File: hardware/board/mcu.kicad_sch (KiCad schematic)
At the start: 22 parts

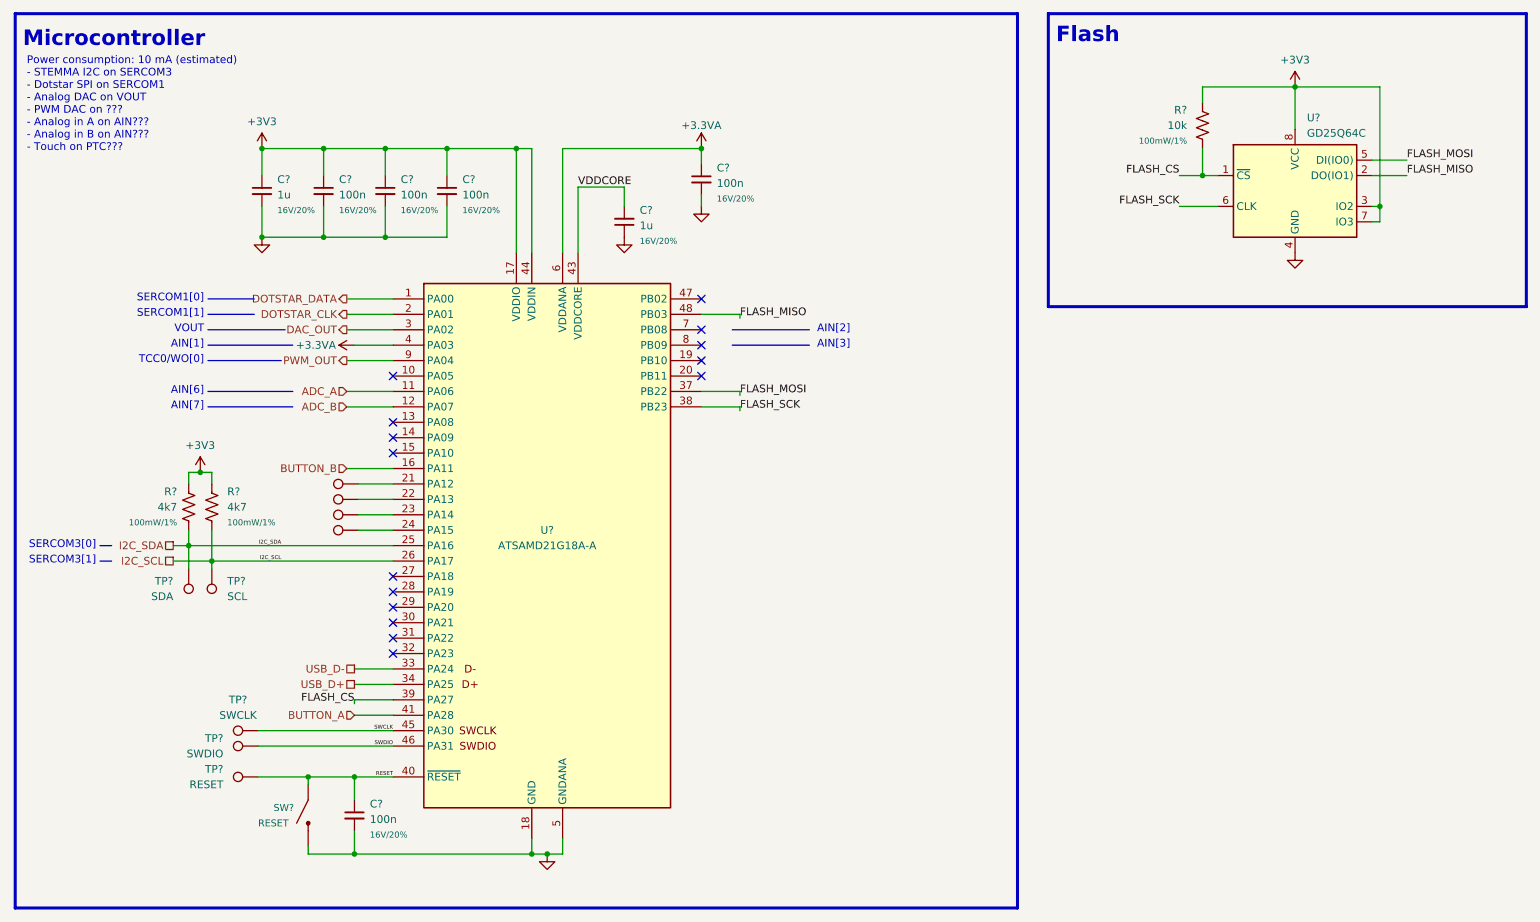
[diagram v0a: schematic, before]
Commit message: hardware: change USB connector, change flash chip, change SPI flash pin assignments, other small updates to routing
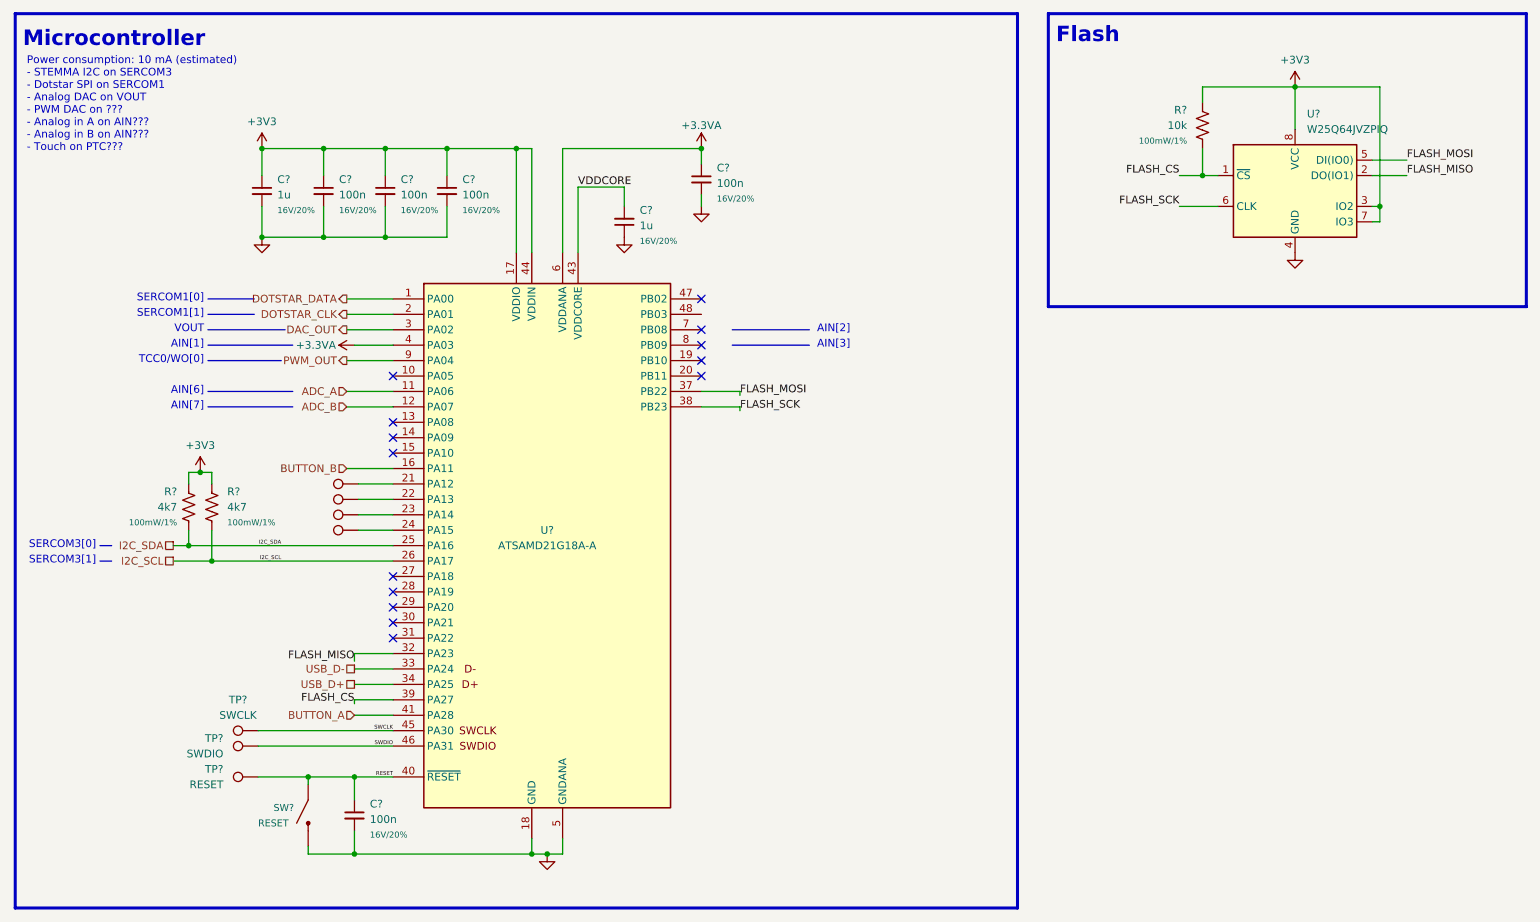
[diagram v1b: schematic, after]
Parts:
- removed TP?: SCL, TestPoint:TestPoint_Pad_D1.0mm, symbol Connector:TestPoint
- removed TP?: SDA, TestPoint:TestPoint_Pad_D1.0mm, symbol Connector:TestPoint
- U?: value GD25Q64C -> W25Q64JVZPIQ; footprint Package_SO:SOIC-8_5.23x5.23mm_P1.27mm -> Package_SON:WSON-8-1EP_6x5mm_P1.27mm_EP3.4x4mm; mfn GD25Q64CSIGR -> (none); mpn GD25Q64CSIGR -> W25Q64JVZPIQ
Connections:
- net FLASH_MISO: now also U?.32 (PA23); no longer U?.48 (PB03)
- no-connect marks 15 -> 14
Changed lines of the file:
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@@
   )
   (no_connect (at 128.27 72.39))
-  (no_connect (at 77.47 120.65))
   (no_connect (at 77.47 115.57))
-  (no_connect (at 77.47 118.11))
+  (no_connect (at 77.47 113.03))
   (no_connect (at 77.47 85.09))
   (no_connect (at 77.47 107.95))
@@
   (no_connect (at 77.47 82.55))
   (no_connect (at 77.47 87.63))
-  (no_connect (at 77.47 113.03))
+  (no_connect (at 77.47 118.11))
   (no_connect (at 128.27 67.31))
   (no_connect (at 128.27 69.85))
@@
     (stroke (width 0) (type default))
   )
-  (wire (pts (xy 47.625 106.68) (xy 47.625 105.41))
-    (stroke (width 0) (type default))
-  )
   (wire (pts (xy 128.27 45.085) (xy 128.27 46.99))
     (stroke (width 0) (type default))
@@
     (stroke (width 0) (type default))
   )
-  (wire (pts (xy 134.62 64.77) (xy 128.27 64.77))
+  (wire (pts (xy 71.12 120.65) (xy 77.47 120.65))
     (stroke (width 0) (type default))
   )
@@
     (stroke (width 0.5) (type solid))
   )
-  (wire (pts (xy 43.815 102.87) (xy 43.815 106.68))
-    (stroke (width 0) (type default))
-  )
   (polyline (pts (xy 180.34 162.56) (xy 15.24 162.56))
     (stroke (width 0.5) (type solid))
@@
     (stroke (width 0) (type default))
   )
-  (wire (pts (xy 134.62 64.77) (xy 134.62 65.405))
+  (wire (pts (xy 71.12 120.65) (xy 71.12 121.92))
     (stroke (width 0) (type default))
   )
@@
     (effects (font (size 1.27 1.27)) (justify right bottom))
   )
-  (label "FLASH_MISO" (at 134.62 65.405 0) (fields_autoplaced)
-    (effects (font (size 1.27 1.27)) (justify left bottom))
+  (label "FLASH_MISO" (at 71.12 121.92 180) (fields_autoplaced)
+    (effects (font (size 1.27 1.27)) (justify right bottom))
   )
   (label "FLASH_CS" (at 71.12 128.905 180) (fields_autoplaced)
@@
   (symbol (lib_id "board:GD25Q64C") (at 226.06 44.45 0) (unit 1)
     (in_bom yes) (on_board yes) (dnp no) (fields_autoplaced)
-    (property "Reference" "U?" (at 228.0159 32.385 0)
-      (effects (font (size 1.27 1.27)) (justify left))
-    )
-    (property "Value" "GD25Q64C" (at 228.0159 34.925 0)
-      (effects (font (size 1.27 1.27)) (justify left))
-    )
-    (property "Footprint" "Package_SO:SOIC-8_5.23x5.23mm_P1.27mm" (at 226.06 44.45 0)
-      (effects (font (size 1.27 1.27)) hide)
-    )
-    (property "Datasheet" "http://www.winbond.com/resource-files/w25q32jv%20revg%2003272018%20plus.pdf" (at 226.06 44.45 0)
-      (effects (font (size 1.27 1.27)) hide)
-    )
-    (property "mfn" "GD25Q64CSIGR" (at 226.06 44.45 0)
-      (effects (font (size 1.27 1.27)) hide)
-    )
-    (property "mpn" "GD25Q64CSIGR" (at 226.06 44.45 0)
+    (property "Reference" "U?" (at 228.0159 31.75 0)
+      (effects (font (size 1.27 1.27)) (justify left))
+    )
+    (property "Value" "W25Q64JVZPIQ" (at 228.0159 34.29 0)
+      (effects (font (size 1.27 1.27)) (justify left))
+    )
+    (property "Footprint" "Package_SON:WSON-8-1EP_6x5mm_P1.27mm_EP3.4x4mm" (at 226.06 44.45 0)
+      (effects (font (size 1.27 1.27)) hide)
+    )
+    (property "Datasheet" "https://www.digikey.com/en/products/detail/winbond-electronics/W25Q64JVZPIQ-TR/5803999" (at 226.06 44.45 0)
+      (effects (font (size 1.27 1.27)) hide)
+    )
+    (property "mpn" "W25Q64JVZPIQ" (at 226.06 44.45 0)
       (effects (font (size 1.27 1.27)) hide)
     )
@@
     )
   )
-  (symbol (lib_id "Connector:TestPoint") (at 47.625 106.68 180) (unit 1)
-    (in_bom yes) (on_board yes) (dnp no) (fields_autoplaced)
-    (property "Reference" "TP?" (at 50.165 108.712 0)
-      (effects (font (size 1.27 1.27)) (justify right))
-    )
-    (property "Value" "SCL" (at 50.165 111.252 0)
-      (effects (font (size 1.27 1.27)) (justify right))
-    )
-    (property "Footprint" "TestPoint:TestPoint_Pad_D1.0mm" (at 42.545 106.68 0)
-      (effects (font (size 1.27 1.27)) hide)
-    )
-    (property "Datasheet" "~" (at 42.545 106.68 0)
-      (effects (font (size 1.27 1.27)) hide)
-    )
-    (property "DNP" "1" (at 47.625 106.68 0)
-      (effects (font (size 1.27 1.27)) hide)
-    )
-    (pin "1")
-    (instances
-      (project "mainboard"
-        (path "/6e47ee4f-b36d-4cb2-9b20-31f755e664f7/00000000-0000-0000-0000-00005f09eaa6"
-          (reference "TP?") (unit 1)
-        )
-      )
-      (project "board"
-        (path "/b6435bdf-358d-4f60-91d0-4c61bcbd9a1b/ebb62435-abe7-41d5-9613-c1c599679f3d"
-          (reference "TP6") (unit 1)
-        )
-      )
-    )
-  )
   (symbol (lib_id "Device:C_Small") (at 86.36 44.45 0) (unit 1)
     (in_bom yes) (on_board yes) (dnp no) (fields_autoplaced)
@@
         )
       )
-    )
-  )
-  (symbol (lib_id "Connector:TestPoint") (at 43.815 106.68 180) (unit 1)
-    (in_bom yes) (on_board yes) (dnp no) (fields_autoplaced)
-    (property "Reference" "TP?" (at 41.275 108.712 0)
-      (effects (font (size 1.27 1.27)) (justify left))
-    )
-    (property "Value" "SDA" (at 41.275 111.252 0)
-      (effects (font (size 1.27 1.27)) (justify left))
-    )
-    (property "Footprint" "TestPoint:TestPoint_Pad_D1.0mm" (at 38.735 106.68 0)
-      (effects (font (size 1.27 1.27)) hide)
-    )
-    (property "Datasheet" "~" (at 38.735 106.68 0)
-      (effects (font (size 1.27 1.27)) hide)
-    )
-    (property "DNP" "1" (at 43.815 106.68 0)
-      (effects (font (size 1.27 1.27)) hide)
-    )
-    (pin "1")
-    (instances
-      (project "mainboard"
-        (path "/6e47ee4f-b36d-4cb2-9b20-31f755e664f7/00000000-0000-0000-0000-00005f09eaa6"
-          (reference "TP?") (unit 1)
-        )
-      )
-      (project "board"
-        (path "/b6435bdf-358d-4f60-91d0-4c61bcbd9a1b/ebb62435-abe7-41d5-9613-c1c599679f3d"
-          (reference "TP5") (unit 1)
-        )
-      )

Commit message: hardware: rename to Goosehonk Nebula, prep v7
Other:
- title: Big Honking Button -> Goosehonk Nebula
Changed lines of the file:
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@@
   (paper "USLetter")
   (title_block
-    (title "Big Honking Button")
-    (date "2023-08-02")
-    (rev "v5")
+    (title "Goosehonk Nebula")
+    (date "2023-10-08")
+    (rev "v7")
     (company "Winterbloom")
     (comment 1 "Alethea Flowers")
     (comment 2 "CERN-OHL-P V2")
+    (comment 3 "goose.wntr.dev")
   )
   (junction (at 71.12 140.97) (diameter 0) (color 0 0 0 0)
